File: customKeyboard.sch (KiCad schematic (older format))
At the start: 87 parts

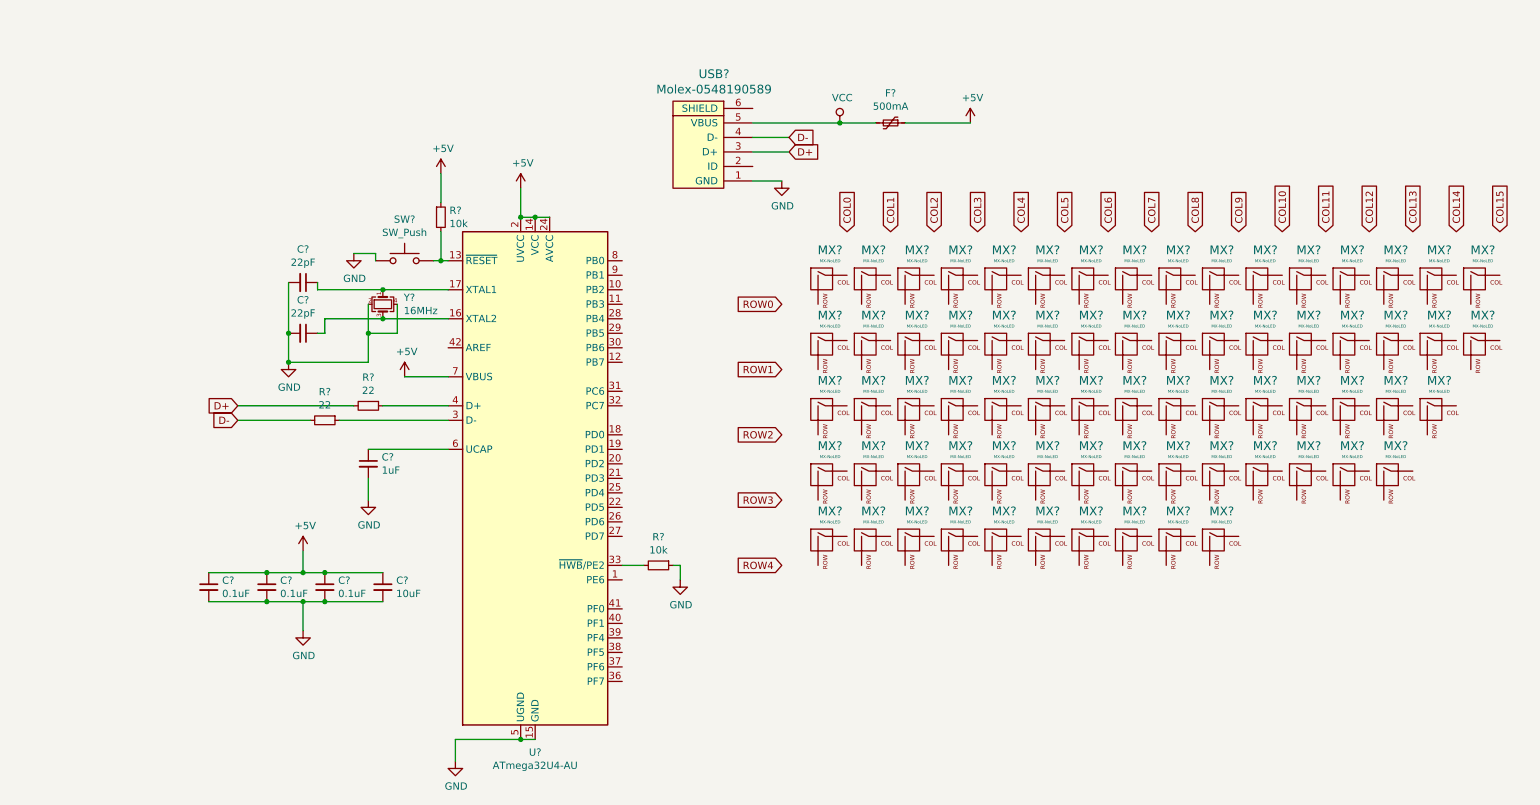
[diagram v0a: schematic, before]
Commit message: Completed Switches Placing
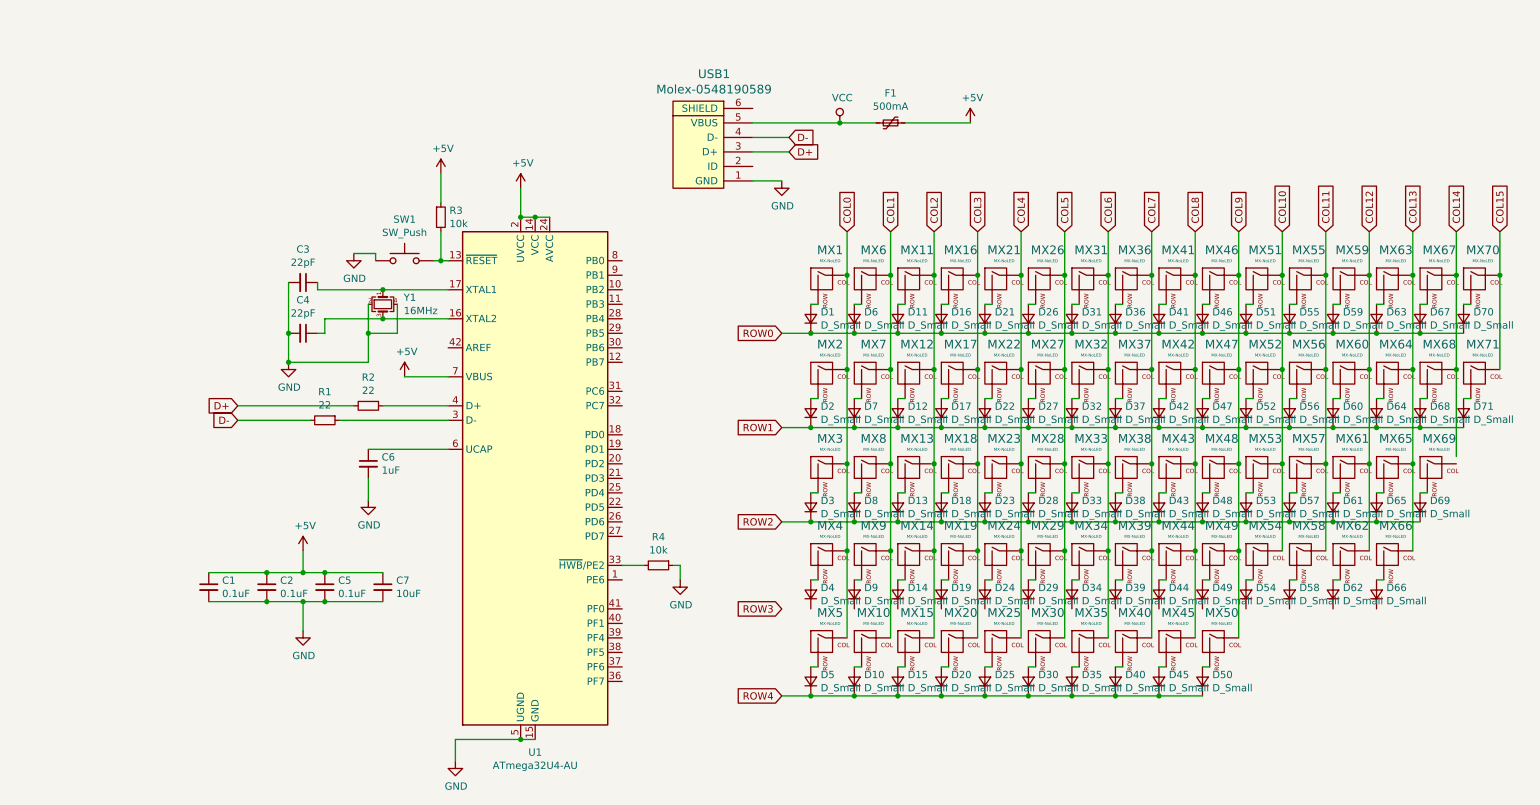
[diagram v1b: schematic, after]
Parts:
- removed MX? (x55): MX-NoLED, symbol MX_Alps_Hybrid:MX-NoLED
- added D1, D10, D11, D12, D13, D14, D15, D16, D17, D18, D19, D2, D20, D21, D22, D23, D24, D25, D26, D27, D28, D29, D3, D30, D31, D32, D33, D34, D35, D36, D37, D38, D39, D4, D40, D41, D42, D43, D44, D45, D46, D47, D48, D49, D5, D50, D51, D52, D53, D54, D55, D56, D57, D58, D59, D6, D60, D61, D62, D63, D64, D65, D66, D67, D68, D69, D7, D70, D71, D8, D9: D_Small, Diode_SMD:D_SOD-123, symbol Device:D_Small
- added MX10, MX12, MX13, MX15, MX18, MX19, MX2, MX20, MX22, MX23, MX24, MX25, MX27, MX28, MX29, MX3, MX32, MX34, MX35, MX37, MX38, MX39, MX4, MX40, MX42, MX43, MX44, MX47, MX49, MX5, MX50, MX52, MX53, MX54, MX56, MX57, MX58, MX60, MX61, MX69, MX7, MX71, MX8, MX9: MX-NoLED, MX_Alps_Hybrid:MX-1U, symbol MX_Alps_Hybrid:MX-NoLED
- added MX14: MX-NoLED, MX_Alps_Hybrid:MX-2U, symbol MX_Alps_Hybrid:MX-NoLED
- added MX17, MX30: MX-NoLED, MX_Alps_Hybrid:MX-1.5U, symbol MX_Alps_Hybrid:MX-NoLED
- added MX33: MX-NoLED, MX_Alps_Hybrid:MX-1.75U, symbol MX_Alps_Hybrid:MX-NoLED
- added MX45, MX48: MX-NoLED, MX_Alps_Hybrid:MX-2.25U, symbol MX_Alps_Hybrid:MX-NoLED
- added MX62, MX64, MX66, MX68: MX-NoLED, MX_Alps_Hybrid:MX-1.25U, symbol MX_Alps_Hybrid:MX-NoLED
- added MX65: MX-NoLED, MX_Alps_Hybrid:MX-6.25U, symbol MX_Alps_Hybrid:MX-NoLED
- C1, C2, C3, C4, C5, C6, C7: renamed from C?; footprint (none) -> Capacitor_SMD:C_0805_2012Metric
- F1: renamed from F?; footprint (none) -> Fuse:Fuse_1206_3216Metric
- MX1, MX11, MX16, MX21, MX26, MX31, MX36, MX41, MX46, MX51, MX55, MX6, MX70: renamed from MX?; footprint (none) -> MX_Alps_Hybrid:MX-1U
- MX59: renamed from MX?; footprint (none) -> MX_Alps_Hybrid:MX-2.75U
- MX63, MX67: renamed from MX?; footprint (none) -> MX_Alps_Hybrid:MX-1.25U
- R1, R2, R3, R4: renamed from R?; footprint (none) -> Resistor_SMD:R_0805_2012Metric
- SW1: renamed from SW?; footprint (none) -> random-keyboard-parts:SKQG-1155865
- USB1: renamed from USB?; footprint (none) -> random-keyboard-parts:Molex-0548190589
- Y1: renamed from Y?; footprint (none) -> Crystal:Crystal_SMD_3225-4Pin_3.2x2.5mm
- gave numbers to parts that had none: 1
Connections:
- net COL0: now also MX1.1 (COL), MX2.1 (COL), MX3.1 (COL), MX4.1 (COL), MX5.1 (COL)
- net COL1: now also MX6.1 (COL), MX10.1 (COL), MX7.1 (COL), MX8.1 (COL), MX9.1 (COL)
- net COL10: now also MX51.1 (COL), MX52.1 (COL), MX53.1 (COL), MX54.1 (COL)
- net COL11: now also MX55.1 (COL), MX56.1 (COL), MX57.1 (COL), MX58.1 (COL)
- net COL12: now also MX59.1 (COL), MX60.1 (COL), MX61.1 (COL), MX62.1 (COL)
- net COL13: now also MX63.1 (COL), MX64.1 (COL), MX65.1 (COL), MX66.1 (COL)
- net COL14: now also MX67.1 (COL), MX68.1 (COL)
- net COL15: now also MX70.1 (COL), MX71.1 (COL)
- net COL2: now also MX11.1 (COL), MX12.1 (COL), MX13.1 (COL), MX14.1 (COL), MX15.1 (COL)
- net COL3: now also MX16.1 (COL), MX17.1 (COL), MX18.1 (COL), MX19.1 (COL), MX20.1 (COL)
- net COL4: now also MX21.1 (COL), MX22.1 (COL), MX23.1 (COL), MX24.1 (COL), MX25.1 (COL)
- net COL5: now also MX26.1 (COL), MX27.1 (COL), MX28.1 (COL), MX29.1 (COL), MX30.1 (COL)
- net COL6: now also MX31.1 (COL), MX32.1 (COL), MX33.1 (COL), MX34.1 (COL), MX35.1 (COL)
- net COL7: now also MX36.1 (COL), MX37.1 (COL), MX38.1 (COL), MX39.1 (COL), MX40.1 (COL)
- net COL8: now also MX41.1 (COL), MX42.1 (COL), MX43.1 (COL), MX44.1 (COL), MX45.1 (COL)
- net COL9: now also MX46.1 (COL), MX47.1 (COL), MX48.1 (COL), MX49.1 (COL), MX50.1 (COL)
- net ROW0: now also D1.1 (K), D11.1 (K), D16.1 (K), D21.1 (K), D26.1 (K), D31.1 (K), D36.1 (K), D41.1 (K), D46.1 (K), D51.1 (K), D55.1 (K), D59.1 (K), D6.1 (K), D63.1 (K), D67.1 (K), D70.1 (K)
- net ROW1: now also D12.1 (K), D17.1 (K), D2.1 (K), D22.1 (K), D27.1 (K), D32.1 (K), D37.1 (K), D42.1 (K), D47.1 (K), D52.1 (K), D56.1 (K), D60.1 (K), D64.1 (K), D68.1 (K), D7.1 (K), D71.1 (K)
- net ROW2: now also D13.1 (K), D18.1 (K), D23.1 (K), D28.1 (K), D3.1 (K), D33.1 (K), D38.1 (K), D43.1 (K), D48.1 (K), D53.1 (K), D57.1 (K), D61.1 (K), D65.1 (K), D69.1 (K), D8.1 (K)
- net ROW4: now also D10.1 (K), D15.1 (K), D20.1 (K), D25.1 (K), D30.1 (K), D35.1 (K), D40.1 (K), D45.1 (K), D5.1 (K), D50.1 (K)
- net at MX1.2 (ROW): now also D1.2 (A)
- net at MX6.2 (ROW): now also D6.2 (A)
- net at MX11.2 (ROW): now also D11.2 (A)
- net at MX16.2 (ROW): now also D16.2 (A)
- net at MX21.2 (ROW): now also D21.2 (A)
- net at MX26.2 (ROW): now also D26.2 (A)
- net at MX31.2 (ROW): now also D31.2 (A)
- net at MX36.2 (ROW): now also D36.2 (A)
- net at MX41.2 (ROW): now also D41.2 (A)
- net at MX46.2 (ROW): now also D46.2 (A)
- net at MX51.2 (ROW): now also D51.2 (A)
- net at MX55.2 (ROW): now also D55.2 (A)
- net at MX59.2 (ROW): now also D59.2 (A)
- net at MX63.2 (ROW): now also D63.2 (A)
- net at MX67.2 (ROW): now also D67.2 (A)
- net at MX70.2 (ROW): now also D70.2 (A)
- new net: D4.2 (A), MX4.2 (ROW)
- new net: D9.2 (A), MX9.2 (ROW)
- new net: D14.2 (A), MX14.2 (ROW)
- new net: D19.2 (A), MX19.2 (ROW)
- new net: D24.2 (A), MX24.2 (ROW)
- new net: D29.2 (A), MX29.2 (ROW)
- new net: D34.2 (A), MX34.2 (ROW)
- new net: D39.2 (A), MX39.2 (ROW)
- new net: D44.2 (A), MX44.2 (ROW)
- new net: D49.2 (A), MX49.2 (ROW)
- new net: D54.2 (A), MX54.2 (ROW)
- new net: D58.2 (A), MX58.2 (ROW)
- new net: D62.2 (A), MX62.2 (ROW)
- new net: D66.2 (A), MX66.2 (ROW)
- new net: D5.2 (A), MX5.2 (ROW)
- new net: D10.2 (A), MX10.2 (ROW)
- new net: D15.2 (A), MX15.2 (ROW)
- new net: D20.2 (A), MX20.2 (ROW)
- new net: D25.2 (A), MX25.2 (ROW)
- new net: D30.2 (A), MX30.2 (ROW)
- new net: D35.2 (A), MX35.2 (ROW)
- new net: D40.2 (A), MX40.2 (ROW)
- new net: D45.2 (A), MX45.2 (ROW)
- new net: D50.2 (A), MX50.2 (ROW)
- new net: D2.2 (A), MX2.2 (ROW)
- new net: D7.2 (A), MX7.2 (ROW)
- new net: D12.2 (A), MX12.2 (ROW)
- new net: D17.2 (A), MX17.2 (ROW)
- new net: D22.2 (A), MX22.2 (ROW)
- new net: D27.2 (A), MX27.2 (ROW)
- new net: D32.2 (A), MX32.2 (ROW)
- new net: D37.2 (A), MX37.2 (ROW)
- new net: D42.2 (A), MX42.2 (ROW)
- new net: D47.2 (A), MX47.2 (ROW)
- new net: D52.2 (A), MX52.2 (ROW)
- new net: D56.2 (A), MX56.2 (ROW)
- new net: D60.2 (A), MX60.2 (ROW)
- new net: D64.2 (A), MX64.2 (ROW)
- new net: D68.2 (A), MX68.2 (ROW)
- new net: D71.2 (A), MX71.2 (ROW)
- new net: D3.2 (A), MX3.2 (ROW)
- new net: D8.2 (A), MX8.2 (ROW)
- new net: D13.2 (A), MX13.2 (ROW)
- new net: D18.2 (A), MX18.2 (ROW)
- new net: D23.2 (A), MX23.2 (ROW)
- new net: D28.2 (A), MX28.2 (ROW)
- new net: D33.2 (A), MX33.2 (ROW)
- new net: D38.2 (A), MX38.2 (ROW)
- new net: D43.2 (A), MX43.2 (ROW)
- new net: D48.2 (A), MX48.2 (ROW)
- new net: D53.2 (A), MX53.2 (ROW)
- new net: D57.2 (A), MX57.2 (ROW)
- new net: D61.2 (A), MX61.2 (ROW)
- new net: D65.2 (A), MX65.2 (ROW)
- new net: D69.2 (A), MX69.2 (ROW)

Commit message: Placing complete and Replaced USB-C
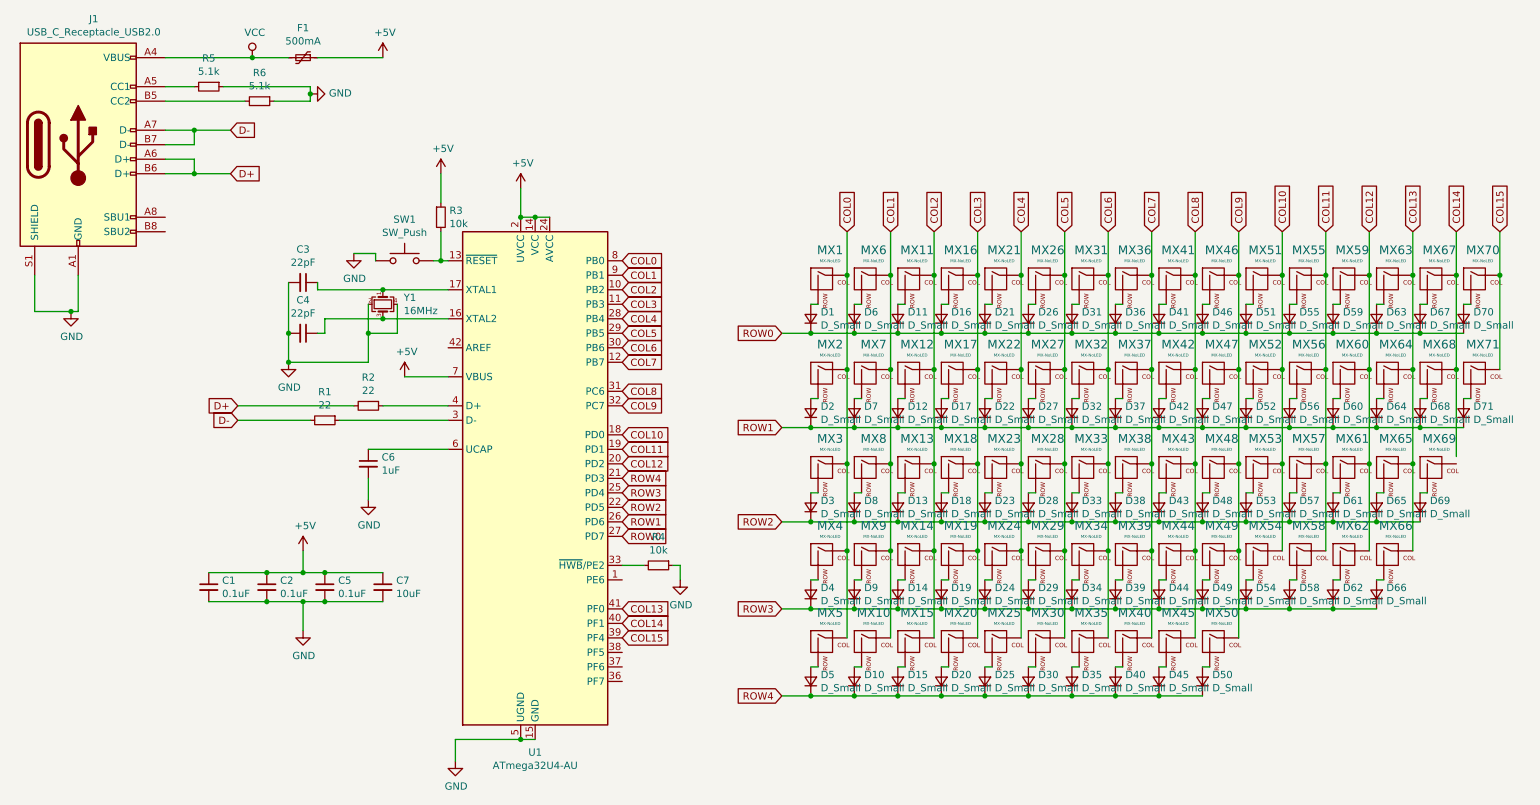
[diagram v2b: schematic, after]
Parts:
- removed USB1: Molex-0548190589, random-keyboard-parts:Molex-0548190589, symbol random-keyboard-parts:Molex-0548190589
- added J1: USB_C_Receptacle_USB2.0, Connector_USB:USB_C_Receptacle_Amphenol_12401548E4-2A, symbol Connector:USB_C_Receptacle_USB2.0
- added R5, R6: 5.1k, Resistor_SMD:R_0805_2012Metric, symbol Device:R_Small
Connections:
- net COL0: now also U1.8 (PB0)
- net COL1: now also U1.9 (PB1)
- net COL10: now also U1.18 (PD0)
- net COL11: now also U1.19 (PD1)
- net COL12: now also U1.20 (PD2)
- net COL13: now also U1.41 (PF0)
- net COL14: now also U1.40 (PF1)
- net COL15: now also U1.39 (PF4)
- net COL2: now also U1.10 (PB2)
- net COL3: now also U1.11 (PB3)
- net COL4: now also U1.28 (PB4)
- net COL5: now also U1.29 (PB5)
- net COL6: now also U1.30 (PB6)
- net COL7: now also U1.12 (PB7)
- net COL8: now also U1.31 (PC6)
- net COL9: now also U1.32 (PC7)
- net D+: now also J1.A6 (D+), J1.B6 (D+)
- net D-: now also J1.A7 (D-), J1.B7 (D-)
- net GND: now also J1.A1 (GND), J1.A12 (GND), J1.B1 (GND), J1.B12 (GND), J1.S1 (SHIELD), R5.1, R6.1
- net ROW0: now also U1.27 (PD7)
- net ROW1: now also U1.26 (PD6)
- net ROW2: now also U1.22 (PD5)
- net ROW3: now also D14.1 (K), D19.1 (K), D24.1 (K), D29.1 (K), D34.1 (K), D39.1 (K), D4.1 (K), D44.1 (K), D49.1 (K), D54.1 (K), D58.1 (K), D62.1 (K), D66.1 (K), D9.1 (K), U1.25 (PD4)
- net ROW4: now also U1.21 (PD3)
- net VCC: now also J1.A4 (VBUS), J1.A9 (VBUS), J1.B4 (VBUS), J1.B9 (VBUS)
- new net: J1.A5 (CC1), R5.2
- new net: J1.B5 (CC2), R6.2
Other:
- moved on the sheet: F1
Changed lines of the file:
@@
 	2700 3350 2200 3350
-$Comp
-L random-keyboard-parts:Molex-0548190589 USB1
-U 1 1 63886A70
-P 5450 1500
-F 0 "USB1" V 5987 1467 60  0000 C CNN
-F 1 "Molex-0548190589" V 5881 1467 60  0000 C CNN
-F 2 "random-keyboard-parts:Molex-0548190589" H 5450 1500 60  0001 C CNN
-F 3 "" H 5450 1500 60  0001 C CNN
-	1    5450 1500
-	0    -1   -1   0
-$EndComp
 $Comp
 L power:VCC #PWR0110
 U 1 1 63889DF8
-P 6350 1300
-F 0 "#PWR0110" H 6350 1150 50  0001 C CNN
-F 1 "VCC" H 6367 1473 50  0000 C CNN
-F 2 "" H 6350 1300 50  0001 C CNN
-F 3 "" H 6350 1300 50  0001 C CNN
-	1    6350 1300
-	1    0    0    -1
-$EndComp
-Wire Wire Line
-	5750 1300 6350 1300
+P 2300 850
+F 0 "#PWR0110" H 2300 700 50  0001 C CNN
+F 1 "VCC" H 2317 1023 50  0000 C CNN
+F 2 "" H 2300 850 50  0001 C CNN
+F 3 "" H 2300 850 50  0001 C CNN
+	1    2300 850
+	1    0    0    -1
+$EndComp
+Wire Wire Line
+	1700 850  2300 850
 $Comp
 L Device:Polyfuse_Small F1
 U 1 1 6388E7A8
-P 6700 1300
-F 0 "F1" V 6495 1300 50  0000 C CNN
-F 1 "500mA" V 6586 1300 50  0000 C CNN
-F 2 "Fuse:Fuse_1206_3216Metric" H 6750 1100 50  0001 L CNN
-F 3 "~" H 6700 1300 50  0001 C CNN
-	1    6700 1300
+P 2650 850
+F 0 "F1" V 2445 850 50  0000 C CNN
+F 1 "500mA" V 2536 850 50  0000 C CNN
+F 2 "Fuse:Fuse_1206_3216Metric" H 2700 650 50  0001 L CNN
+F 3 "~" H 2650 850 50  0001 C CNN
+	1    2650 850
 	0    1    1    0
 $EndComp
@@
 L power:+5V #PWR0111
 U 1 1 6388F728
-P 7250 1300
-F 0 "#PWR0111" H 7250 1150 50  0001 C CNN
-F 1 "+5V" H 7265 1473 50  0000 C CNN
-F 2 "" H 7250 1300 50  0001 C CNN
-F 3 "" H 7250 1300 50  0001 C CNN
-	1    7250 1300
-	1    0    0    -1
-$EndComp
-Wire Wire Line
-	6350 1300 6600 1300
-Connection ~ 6350 1300
-Wire Wire Line
-	6800 1300 7250 1300
-Text GLabel 6000 1400 2    50   Input ~ 0
+P 3200 850
+F 0 "#PWR0111" H 3200 700 50  0001 C CNN
+F 1 "+5V" H 3215 1023 50  0000 C CNN
+F 2 "" H 3200 850 50  0001 C CNN
+F 3 "" H 3200 850 50  0001 C CNN
+	1    3200 850
+	1    0    0    -1
+$EndComp
+Wire Wire Line
+	2300 850  2550 850
+Connection ~ 2300 850
+Wire Wire Line
+	2750 850  3200 850
+Text GLabel 2150 1350 2    50   Input ~ 0
 D-
-Text GLabel 6000 1500 2    50   Input ~ 0
+Text GLabel 2150 1650 2    50   Input ~ 0
 D+
-Wire Wire Line
-	5750 1400 6000 1400
-Wire Wire Line
-	5750 1500 6000 1500
 $Comp
 L power:GND #PWR0112
 U 1 1 63894070
-P 5950 1700
-F 0 "#PWR0112" H 5950 1450 50  0001 C CNN
-F 1 "GND" H 5955 1527 50  0000 C CNN
-F 2 "" H 5950 1700 50  0001 C CNN
-F 3 "" H 5950 1700 50  0001 C CNN
-	1    5950 1700
-	1    0    0    -1
-$EndComp
-Wire Wire Line
-	5750 1700 5950 1700
+P 1050 2600
+F 0 "#PWR0112" H 1050 2350 50  0001 C CNN
+F 1 "GND" H 1055 2427 50  0000 C CNN
+F 2 "" H 1050 2600 50  0001 C CNN
+F 3 "" H 1050 2600 50  0001 C CNN
+	1    1050 2600
+	1    0    0    -1
+$EndComp
 $Comp
 L MX_Alps_Hybrid:MX-NoLED MX1
@@
 	10900 2350 10900 2050
 Connection ~ 10900 2350
+Wire Wire Line
+	5950 4650 6150 4650
+Wire Wire Line
+	6150 4650 6450 4650
+Connection ~ 6150 4650
+Wire Wire Line
+	6450 4650 6750 4650
+Connection ~ 6450 4650
+Wire Wire Line
+	6750 4650 7050 4650
+Connection ~ 6750 4650
+Wire Wire Line
+	7050 4650 7350 4650
+Connection ~ 7050 4650
+Wire Wire Line
+	7350 4650 7650 4650
+Connection ~ 7350 4650
+Wire Wire Line
+	7650 4650 7950 4650
+Connection ~ 7650 4650
+Wire Wire Line
+	7950 4650 8250 4650
+Connection ~ 7950 4650
+Wire Wire Line
+	8250 4650 8550 4650
+Connection ~ 8250 4650
+Wire Wire Line
+	8550 4650 8850 4650
+Connection ~ 8550 4650
+Wire Wire Line
+	8850 4650 9150 4650
+Connection ~ 8850 4650
+Wire Wire Line
+	9150 4650 9450 4650
+Connection ~ 9150 4650
+Wire Wire Line
+	9450 4650 9750 4650
+Connection ~ 9450 4650
+Wire Wire Line
+	10050 4650 9750 4650
+Connection ~ 9750 4650
+$Comp
+L Connector:USB_C_Receptacle_USB2.0 J1
+U 1 1 63A0586A
+P 1100 1450
+F 0 "J1" H 1207 2317 50  0000 C CNN
+F 1 "USB_C_Receptacle_USB2.0" H 1207 2226 50  0000 C CNN
+F 2 "Connector_USB:USB_C_Receptacle_Amphenol_12401548E4-2A" H 1250 1450 50  0001 C CNN
+F 3 "https://www.usb.org/sites/default/files/documents/usb_type-c.zip" H 1250 1450 50  0001 C CNN
+	1    1100 1450
+	1    0    0    -1
+$EndComp
+Wire Wire Line
+	800  2350 800  2600
+Wire Wire Line
+	800  2600 1050 2600
+Wire Wire Line
+	1100 2350 1100 2600
+Wire Wire Line
+	1100 2600 1050 2600
+Connection ~ 1050 2600
+Wire Wire Line
+	1700 1350 1900 1350
+Wire Wire Line
+	1700 1450 1900 1450
+Wire Wire Line
+	1900 1450 1900 1350
+Connection ~ 1900 1350
+Wire Wire Line
+	1900 1350 2150 1350
+Wire Wire Line
+	1700 1650 1900 1650
+Wire Wire Line
+	1700 1550 1900 1550
+Wire Wire Line
+	1900 1550 1900 1650
+Connection ~ 1900 1650
+Wire Wire Line
+	1900 1650 2150 1650
+$Comp
+L Device:R_Small R5
+U 1 1 63B37481
+P 2000 1050
+F 0 "R5" V 1804 1050 50  0000 C CNN
+F 1 "5.1k" V 1895 1050 50  0000 C CNN
+F 2 "Resistor_SMD:R_0805_2012Metric" H 2000 1050 50  0001 C CNN
+F 3 "~" H 2000 1050 50  0001 C CNN
+	1    2000 1050
+	0    1    1    0
+$EndComp
+$Comp
+L Device:R_Small R6
+U 1 1 63B39EE6
+P 2350 1150
+F 0 "R6" V 2154 1150 50  0000 C CNN
+F 1 "5.1k" V 2245 1150 50  0000 C CNN
+F 2 "Resistor_SMD:R_0805_2012Metric" H 2350 1150 50  0001 C CNN
+F 3 "~" H 2350 1150 50  0001 C CNN
+	1    2350 1150
+	0    1    1    0
+$EndComp
+$Comp
+L power:GND #PWR0114
+U 1 1 63B4F962
+P 2700 1100
+F 0 "#PWR0114" H 2700 850 50  0001 C CNN
+F 1 "GND" V 2705 972 50  0000 R CNN
+F 2 "" H 2700 1100 50  0001 C CNN
+F 3 "" H 2700 1100 50  0001 C CNN
+	1    2700 1100
+	0    -1   -1   0
+$EndComp
+Wire Wire Line
+	1700 1050 1900 1050
+Wire Wire Line
+	2100 1050 2700 1050
+Wire Wire Line
+	2700 1050 2700 1100
+Wire Wire Line
+	2250 1150 1700 1150
+Wire Wire Line
+	2450 1150 2700 1150
+Wire Wire Line
+	2700 1150 2700 1100
+Connection ~ 2700 1100
+Text GLabel 4850 4150 2    50   Input ~ 0
+ROW0
+Text GLabel 4850 4050 2    50   Input ~ 0
+ROW1
+Text GLabel 4850 3950 2    50   Input ~ 0
+ROW2
+Text GLabel 4850 3850 2    50   Input ~ 0
+ROW3
+Text GLabel 4850 3750 2    50   Input ~ 0
+ROW4
+Text GLabel 4850 2250 2    50   Input ~ 0
+COL0
+Text GLabel 4850 2350 2    50   Input ~ 0
+COL1
+Text GLabel 4850 2450 2    50   Input ~ 0
+COL2
+Text GLabel 4850 2550 2    50   Input ~ 0
+COL3
+Text GLabel 4850 2650 2    50   Input ~ 0
+COL4
+Text GLabel 4850 2750 2    50   Input ~ 0
+COL5
+Text GLabel 4850 2850 2    50   Input ~ 0
+COL6
+Text GLabel 4850 2950 2    50   Input ~ 0
+COL7
+Text GLabel 4850 3150 2    50   Input ~ 0
+COL8
+Text GLabel 4850 3250 2    50   Input ~ 0
+COL9
+Text GLabel 4850 3450 2    50   Input ~ 0
+COL10
+Text GLabel 4850 3550 2    50   Input ~ 0
+COL11
+Text GLabel 4850 3650 2    50   Input ~ 0
+COL12
+Text GLabel 4850 4650 2    50   Input ~ 0
+COL13
+Text GLabel 4850 4750 2    50   Input ~ 0
+COL14
+Text GLabel 4850 4850 2    50   Input ~ 0
+COL15
 $EndSCHEMATC
